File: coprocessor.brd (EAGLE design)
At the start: 160 x 100 mm, 1 part, among them IC1 ATMEGA32U2-TQFP

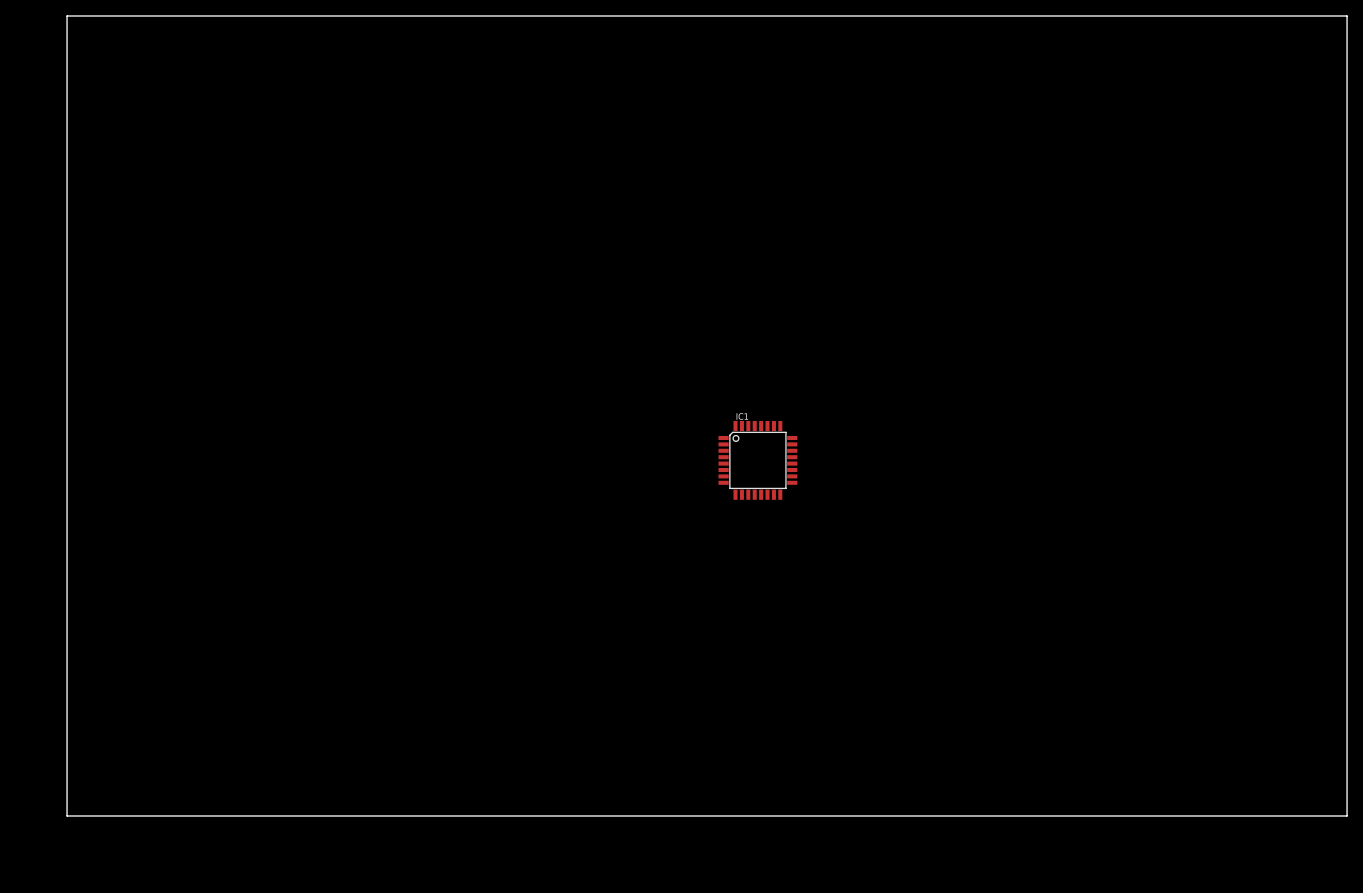
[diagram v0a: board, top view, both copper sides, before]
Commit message: added the co-processor and whatnot
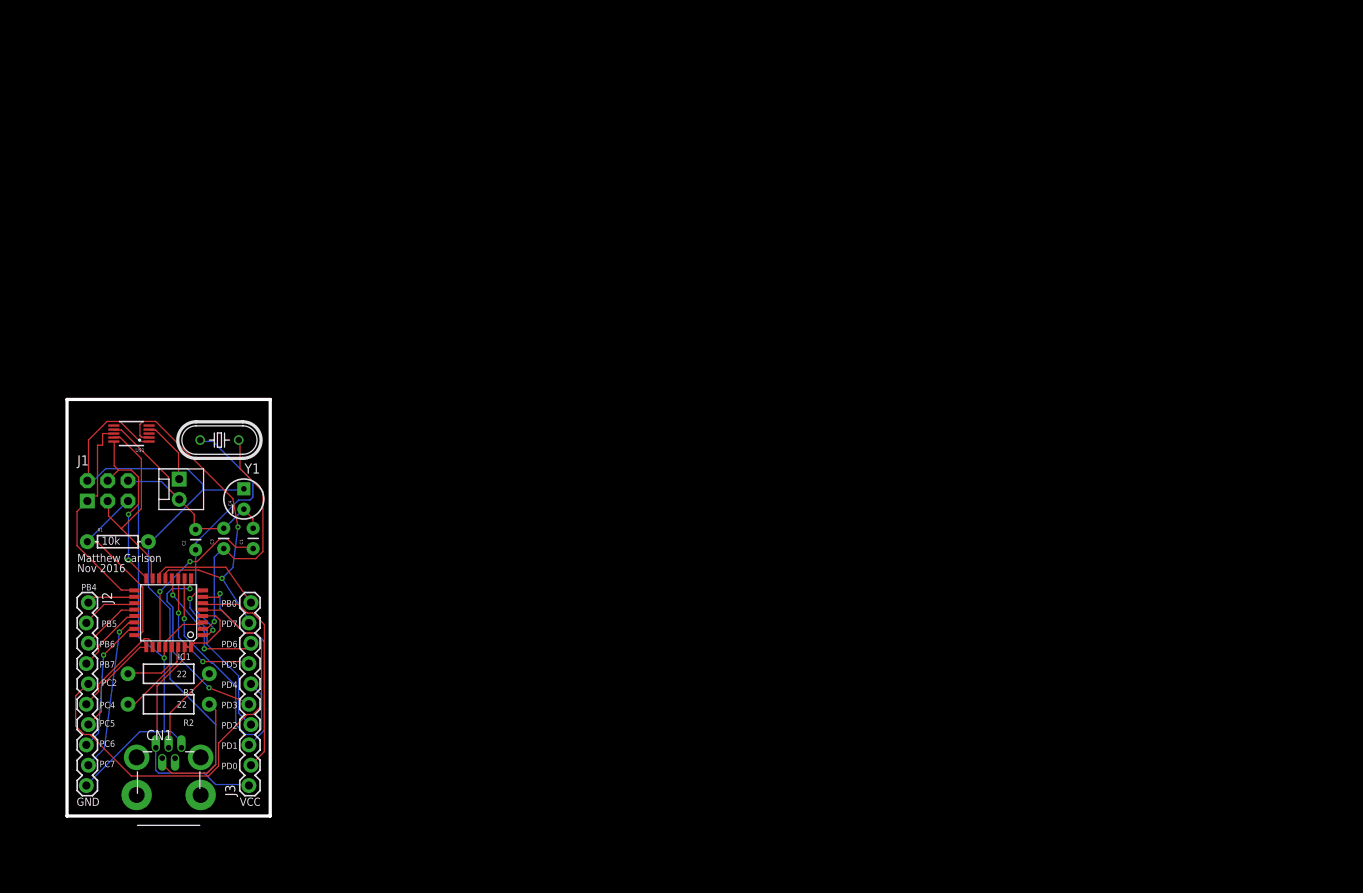
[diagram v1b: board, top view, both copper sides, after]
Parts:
- added C1: 1uF, SparkFun-Capacitors:CAP-PTH-SMALL
- added C2, C3: 22pF, SparkFun-Capacitors:CAP-PTH-SMALL
- added C4: 10uF, SparkFun-Capacitors:CPOL-RADIAL-10UF-25V
- added CN1: (no value), adafruit:USB-MINIB-THM
- added J1: (no value), SparkFun-Connectors:2X3-NS
- added J2, J3: (no value), SparkFun-Connectors:1X10_LOCK
- added J4: (no value), SparkFun-Connectors:MOLEX-1X2
- added R1: 10k, SparkFun-Resistors:AXIAL-0.3EZ
- added R2, R3: 22, SparkFun-Resistors:AXIAL-0.4
- added U$1: MCP48FEB01-E/UN, custom:10-MSOP
- added Y1: 16MHZ, SparkFun-FreqCtrl:HC49U-V
- IC1: value ATMEGA32U2-TQFP -> MEGA32U2
- moved IC1 76.1 mm to (12.7, 25.4), turned to 180 degrees
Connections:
- new net DAC_VOUT: J4.1, U$1.4
- new net GND: C1.2, C2.2, C3.2, C4.2, CN1.GND, IC1.28, IC1.3, J1.6, J2.10, J4.2, U$1.7
- new net MISO: IC1.17, J1.1, U$1.8
- new net MOSI: IC1.16, J1.4, U$1.10
- new net N$10: C3.1, IC1.2, Y1.1
- new net N$4: IC1.29, R3.P$2
- new net N$5: IC1.30, R2.P$2
- new net N$6: CN1.D+, R3.P$1
- new net N$7: C1.1, IC1.27
- new net N$8: CN1.D-, R2.P$1
- new net N$9: C2.1, IC1.1, Y1.2
- new net PB0: IC1.14, J3.10
- new net PB4: IC1.18, J2.1
- new net PB5: IC1.19, J2.2
- new net PB6: IC1.20, J2.3
- new net PB7: IC1.21, J2.4
- new net PC2: IC1.5, J2.5
- new net PC4: IC1.26, J2.6
- new net PC5: IC1.25, J2.7
- new net PC6: IC1.23, J2.8
- new net PC7: IC1.22, J2.9
- new net PD0: IC1.6, J3.2
- new net PD1: IC1.7, J3.3
- new net PD2: IC1.8, J3.4
- new net PD3: IC1.9, J3.5
- new net PD4: IC1.10, J3.6
- new net PD5: IC1.11, J3.7
- new net PD6: IC1.12, J3.8
- new net PD7: IC1.13, J3.9, U$1.2
- new net RESET: IC1.24, J1.5, R1.P$1
- new net SCK: IC1.15, J1.3, U$1.9
- new net VCC: C4.1, CN1.VBUS, IC1.31, IC1.32, IC1.4, J1.2, J3.1, R1.P$2, U$1.1
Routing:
- net VCC: track 0.00 -> 117.5 mm
- net GND: track 0.00 -> 91.3 mm, vias 0 -> 1
- net PC2: track 0.00 -> 54.3 mm
- net PD7: track 0.00 -> 43.8 mm, vias 0 -> 2
- net N$9: track 0.00 -> 33.5 mm, vias 0 -> 1
- net N$10: track 0.00 -> 32.4 mm, vias 0 -> 1
- net PD4: track 0.00 -> 31.2 mm, vias 0 -> 1
- net MISO: track 0.00 -> 27.3 mm
- net PD0: track 0.00 -> 27.0 mm
- net SCK: track 0.00 -> 26.4 mm
- net PD1: track 0.00 -> 25.3 mm, vias 0 -> 1
- net PD3: track 0.00 -> 23.9 mm, vias 0 -> 2
- net RESET: track 0.00 -> 23.3 mm
- net MOSI: track 0.00 -> 22.7 mm, vias 0 -> 2
- net N$7: track 0.00 -> 22.0 mm, vias 0 -> 2
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- added copper zone on layer 1, net GND
- added copper zone on layer 16, net GND
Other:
- board size 160 x 100 mm -> 25.4 x 52.1 mm
- board text added: "GND"
- board text added: "Matthew Carlson"
- board text added: "Nov 2016"
- board text added: "PB0"
- board text added: "PB4"
- board text added: "PB5"
- board text added: "PB6"
- board text added: "PB7"
- board text added: "PC2"
- board text added: "PC4"
- board text added: "PC5"
- board text added: "PC6"
- board text added: "PC7"
- board text added: "PD0"
- board text added: "PD1"
- board text added: "PD2"
- board text added: "PD3"
- board text added: "PD4"
- board text added: "PD5"
- board text added: "PD6"
- board text added: "PD7"
- board text added: "VCC"

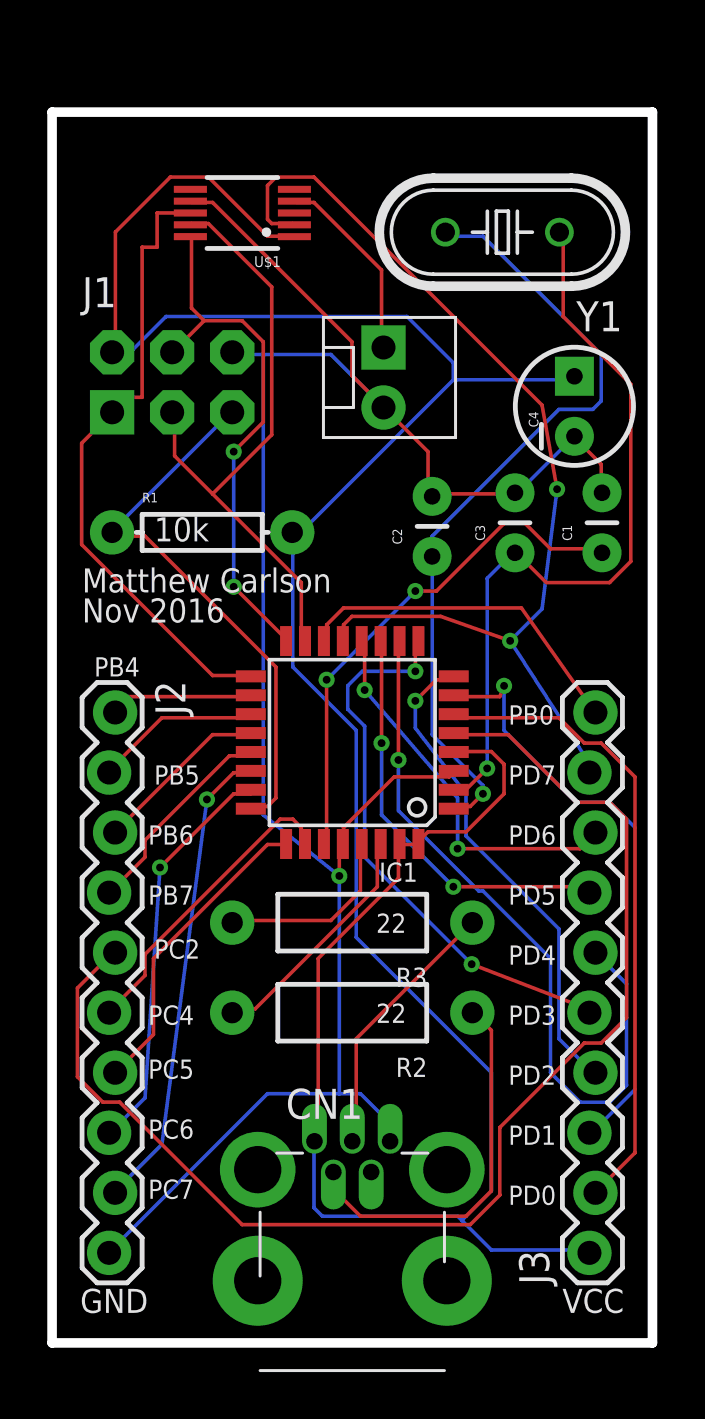
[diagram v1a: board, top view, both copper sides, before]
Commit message: Changed the clearances to match 12 mils at shop
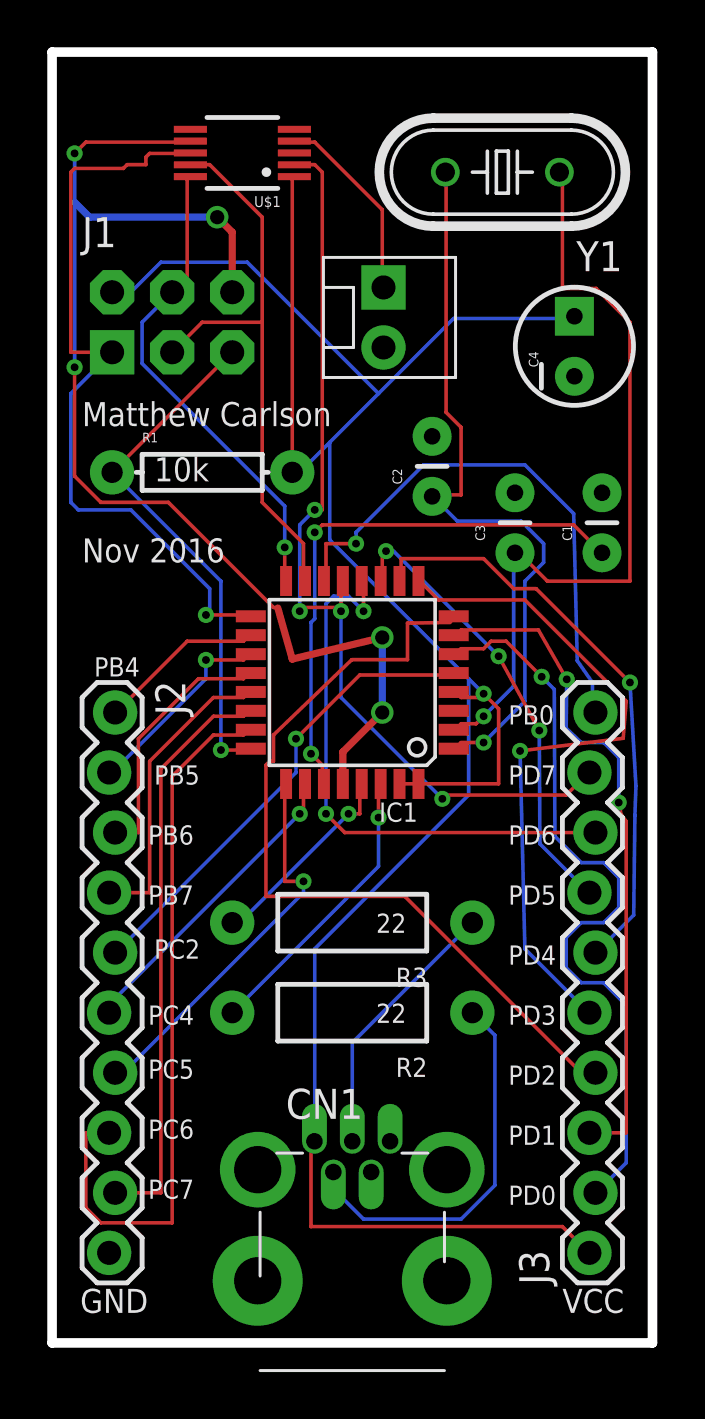
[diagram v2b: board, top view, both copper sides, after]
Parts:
- moved IC1 2.54 mm to (12.7, 27.9)
- moved C2 2.54 mm to (16.1, 35.8)
- moved C4 2.54 mm to (22.1, 42.2)
- moved J1 2.54 mm to (5.08, 43.2)
- moved J4 2.54 mm to (14.0, 44.7)
- moved R1 2.54 mm to (6.35, 36.8)
- moved U$1 2.54 mm to (8.05, 50.3)
- moved Y1 2.54 mm to (19.1, 49.5)
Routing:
- net GND: track 91.3 -> 52.4 mm, vias 1 -> 5
- net PC2: track 54.3 -> 20.1 mm, vias 0 -> 1
- net VCC: track 117.5 -> 102.6 mm, vias 0 -> 1
- net PC6: track 17.2 -> 31.1 mm, vias 1 -> 0
- net PD2: track 20.9 -> 34.7 mm, vias 1 -> 0
- net PB0: track 14.7 -> 23.3 mm, vias 0 -> 1
- net PD6: track 16.5 -> 23.9 mm
- net PD4: track 31.2 -> 24.9 mm
- net PD3: track 23.9 -> 29.1 mm, vias 2 -> 1
- net MISO: track 27.3 -> 32.5 mm, vias 0 -> 1
- net PD0: track 27.0 -> 31.9 mm, vias 0 -> 1
- net PC7: track 20.0 -> 24.7 mm, vias 1 -> 0
- net PB7: track 8.96 -> 12.8 mm
- net PD7: track 43.8 -> 40.0 mm, vias 2 -> 4
- net PC5: track 13.1 -> 16.5 mm, vias 0 -> 1
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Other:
- board size 25.4 x 52.1 mm -> 25.4 x 54.6 mm

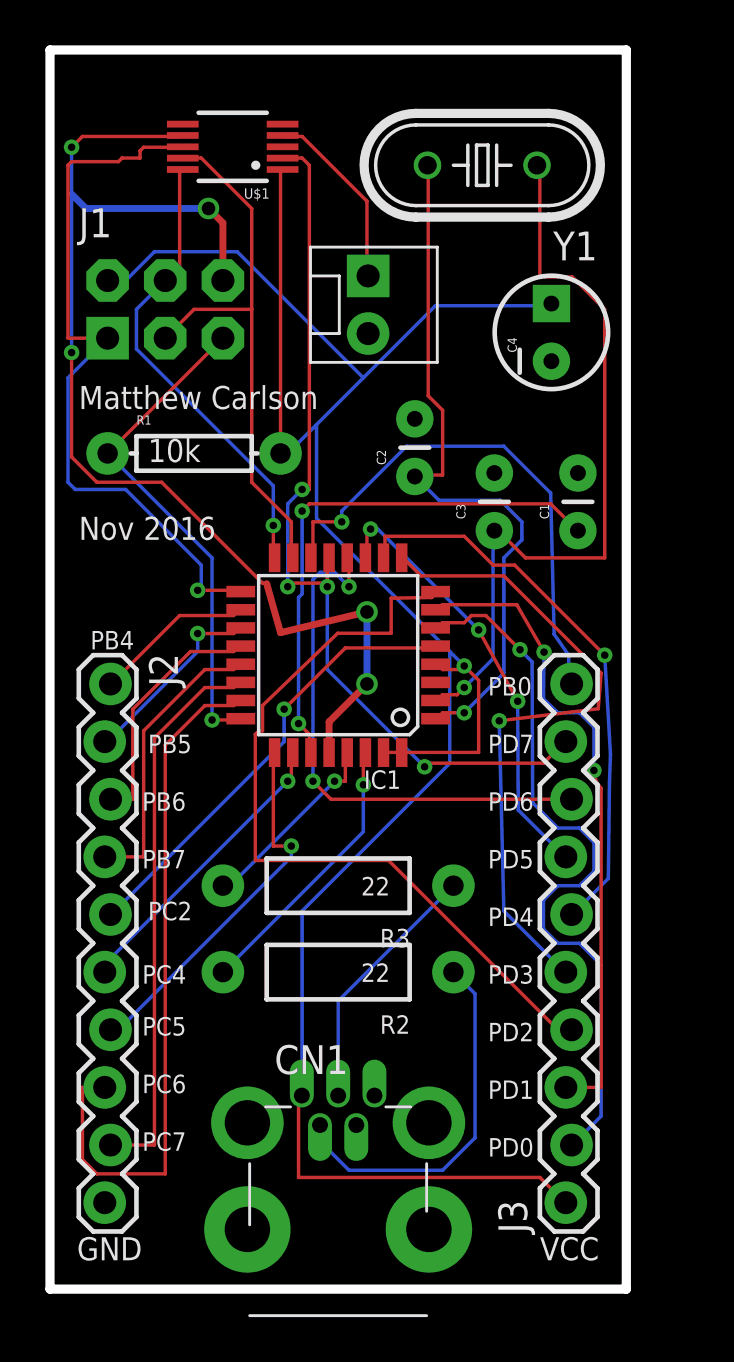
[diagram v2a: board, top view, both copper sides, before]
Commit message: redid the routing by hand
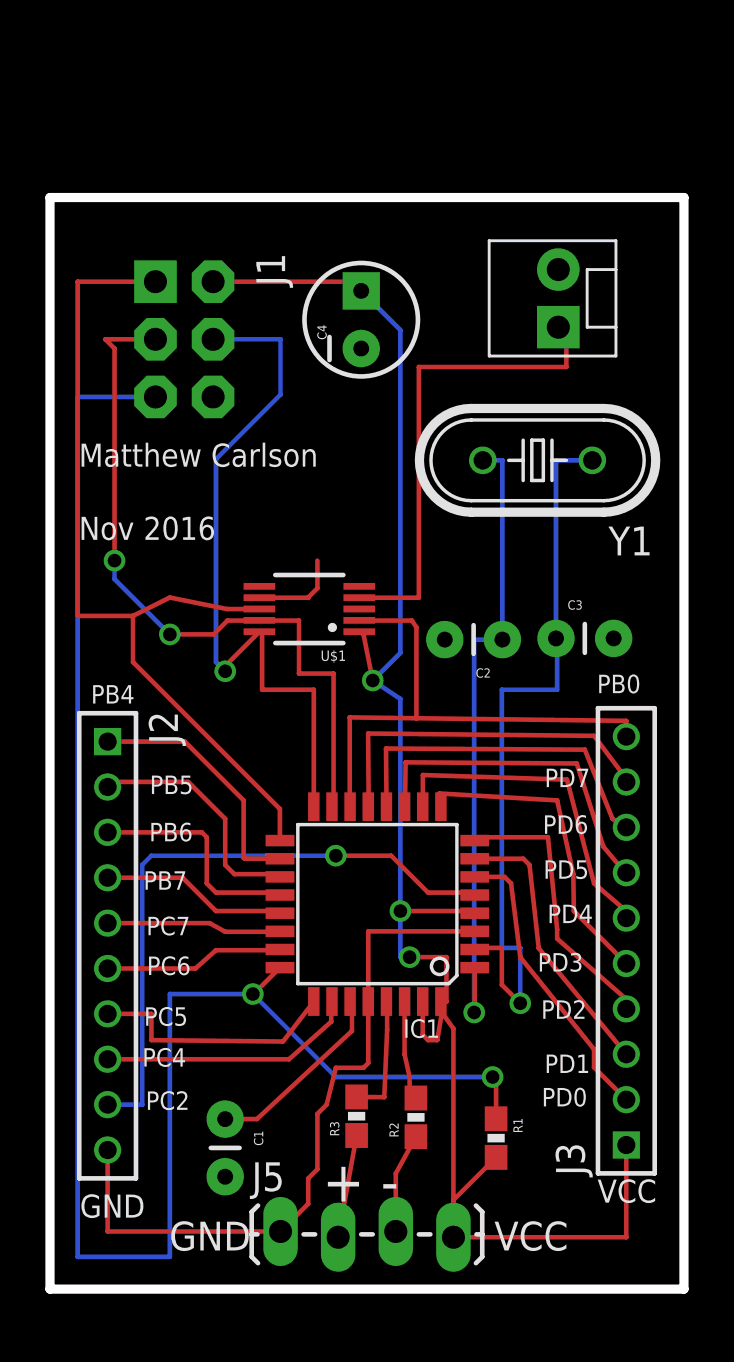
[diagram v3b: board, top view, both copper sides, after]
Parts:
- removed CN1: (no value), adafruit:USB-MINIB-THM
- added J5: (no value), SparkFun-Connectors:1X04_LOCK_LONGPADS
- J2, J3: device SparkFun-Connectors:1X10_LOCK -> SparkFun-Connectors:1X10-2MM
- R1: device SparkFun-Resistors:AXIAL-0.3EZ -> SparkFun-Resistors:0603-RES
- R2, R3: device SparkFun-Resistors:AXIAL-0.4 -> SparkFun-Resistors:0603-RES
- moved R1 33.0 mm to (19.7, 6.65), turned to 270 degrees
- moved C1 30.2 mm to (7.72, 7.49), turned to 270 degrees
- moved U$1 20.6 mm to (11.4, 30.0)
- moved Y1 13.2 mm to (21.5, 36.5)
- moved IC1 11.1 mm to (14.4, 17.0)
- moved R3 10.2 mm to (13.5, 7.62), turned to 90 degrees
- moved J4 8.68 mm to (22.4, 42.4), turned to 90 degrees
- moved C4 8.40 mm to (13.7, 42.7)
- moved C2 8.16 mm to (19.9, 28.6), turned to 180 degrees
- moved R2 7.26 mm to (16.1, 7.57), turned to 90 degrees
- moved C3 5.47 mm to (22.3, 28.7), turned to 0 degrees
- moved J3 3.59 mm to (25.4, 6.35)
- moved J2 2.54 mm to (2.54, 24.1)
- moved J1 1.56 mm to (5.92, 41.9), turned to 270 degrees
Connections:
- removed net N$5: IC1.30, R2.P$2
- removed net N$6: CN1.D+, R3.P$1
- removed net N$8: CN1.D-, R2.P$1
- new net N$1: J5.2, R3.1
- new net N$2: IC1.29, R3.2
- new net N$3: IC1.30, R2.2
- net GND: now also J5.1; no longer CN1.GND
- net N$4: now also J5.3, R2.1; no longer IC1.29, R3.P$2
- net PB0: now also U$1.2
- net PC2: now also J2.9; no longer J2.5
- net PC4: now also J2.8; no longer J2.6
- net PC6: now also J2.6; no longer J2.8
- net PC7: now also J2.5; no longer J2.9
- net PD7: no longer U$1.2
- net RESET: now also R1.1; no longer R1.P$1
- net VCC: now also J5.4, R1.2; no longer CN1.VBUS, R1.P$2
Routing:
- net RESET: track 22.1 -> 76.3 mm, vias 1 -> 2
- net VCC: track 102.6 -> 77.9 mm, vias 1 -> 3
- net PD7: track 40.0 -> 15.7 mm, vias 4 -> 0
- net PC6: track 31.1 -> 7.91 mm
- net PD2: track 34.7 -> 12.5 mm
- net PD0: track 31.9 -> 13.0 mm, vias 1 -> 0
- net GND: track 52.4 -> 35.3 mm, vias 5 -> 0
- net PC7: track 24.7 -> 7.75 mm
- net N$8: track 16.4 -> 0.00 mm
- net PD1: track 28.4 -> 12.3 mm, vias 2 -> 0
- net N$7: track 23.7 -> 8.42 mm, vias 2 -> 0
- net PD3: track 29.1 -> 14.1 mm, vias 1 -> 0
- net DAC_VOUT: track 8.21 -> 21.4 mm
- net N$5: track 12.3 -> 0.00 mm, vias 1 -> 0
- net N$6: track 11.4 -> 0.00 mm
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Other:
- board size 25.4 x 54.6 mm -> 27.9 x 48.1 mm
- board text added: "+"
- board text added: "-"

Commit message: Finished the coprocessor
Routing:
- added copper zone on layer 16, net N$5
- removed copper zone on layer 16, net GND
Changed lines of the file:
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@@
-<vertex x="0" y="0"/>
-</polygon>
-<polygon width="0.4064" layer="16" isolate="0.4064">
-<vertex x="0" y="48.1076"/>
-<vertex x="27.94" y="48.1076"/>
-<vertex x="27.94" y="0"/>
 <vertex x="0" y="0"/>
 </polygon>
@@
 <wire x1="11.3792" y1="30.48" x2="11.7856" y2="30.8864" width="0.2032" layer="1"/>
 <wire x1="11.7856" y1="30.8864" x2="11.7856" y2="32.1056" width="0.2032" layer="1"/>
+<wire x1="18.7198" y1="15.7672" x2="17.399" y2="28.6258" width="0" layer="19" extent="1-1"/>
 </signal>
 <signal name="RESET">
@@
 <wire x1="4.062" y1="8.13" x2="2.54" y2="8.13" width="0.2032" layer="16"/>
 </signal>
+<signal name="N$5">
+<polygon width="0.4064" layer="16" isolate="0.4064">
+<vertex x="0" y="47.9552"/>
+<vertex x="28.0416" y="47.9552"/>
+<vertex x="28.0416" y="47.5488"/>
+<vertex x="28.0416" y="0"/>
+<vertex x="0" y="0"/>
+<vertex x="0" y="0.4064"/>
+</polygon>
+</signal>
 </signals>
